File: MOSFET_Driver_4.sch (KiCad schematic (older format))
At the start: 20 parts, among them Q10 TPHR8504PL, Q11 TPHR8504PL, Q12 TPHR8504PL, Q7 TPHR8504PL, Q8 TPHR8504PL, Q9 TPHR8504PL, U1 FD6288Q

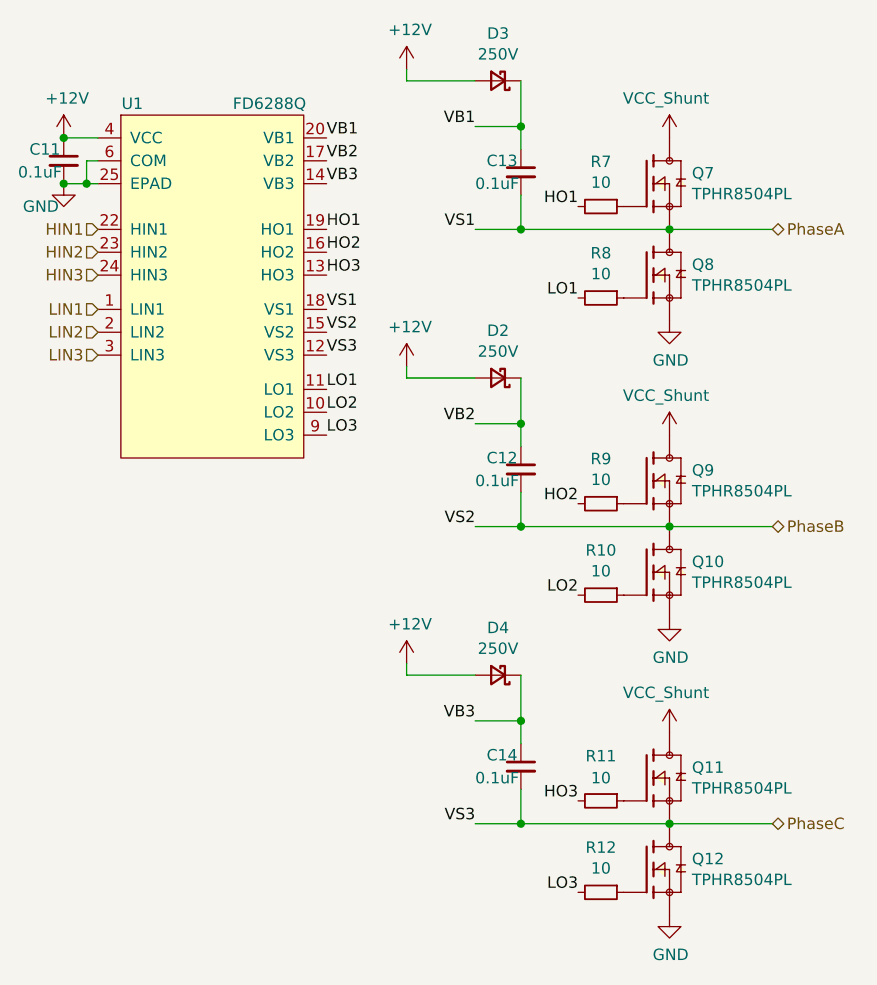
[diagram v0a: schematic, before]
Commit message: Added the rest of the phases and their associated components
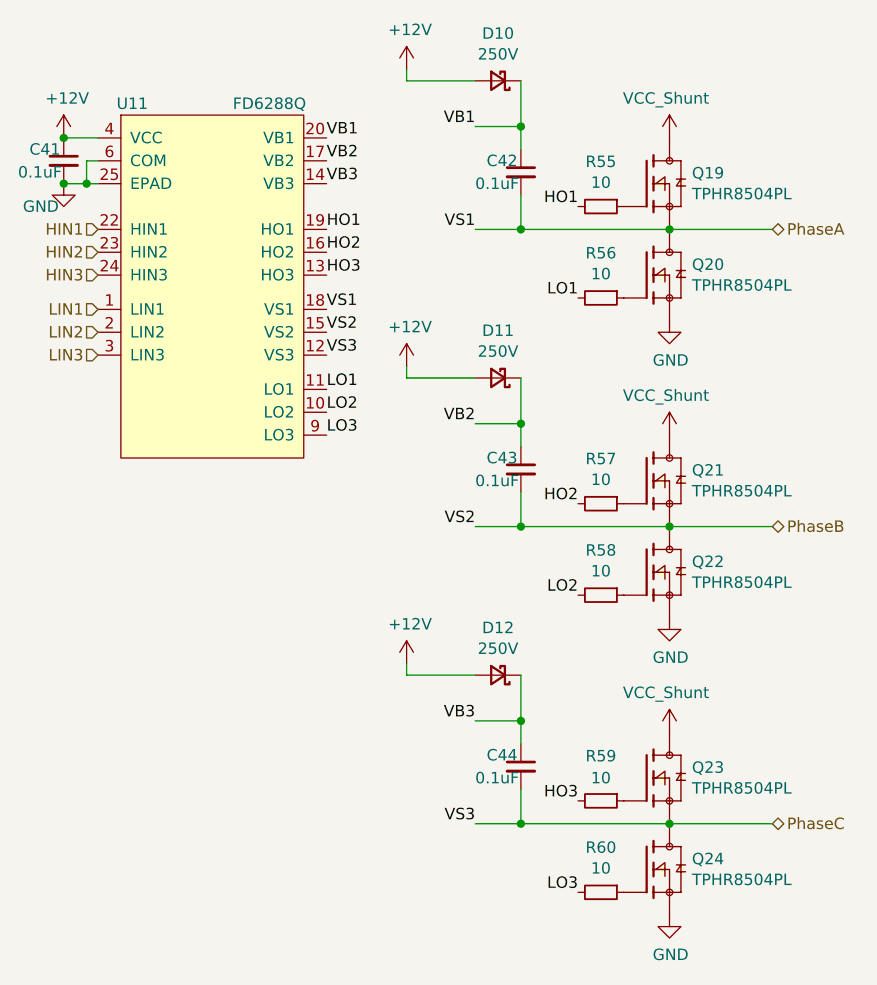
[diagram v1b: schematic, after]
